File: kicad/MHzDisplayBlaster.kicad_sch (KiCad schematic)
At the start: 6 parts, among them J1 Conn_02x15 DigitRHS, J2 Conn_02x15 DigitLHS, J3 Conn_01x03, J4 Conn_01x07, U1 DC56-11GWA

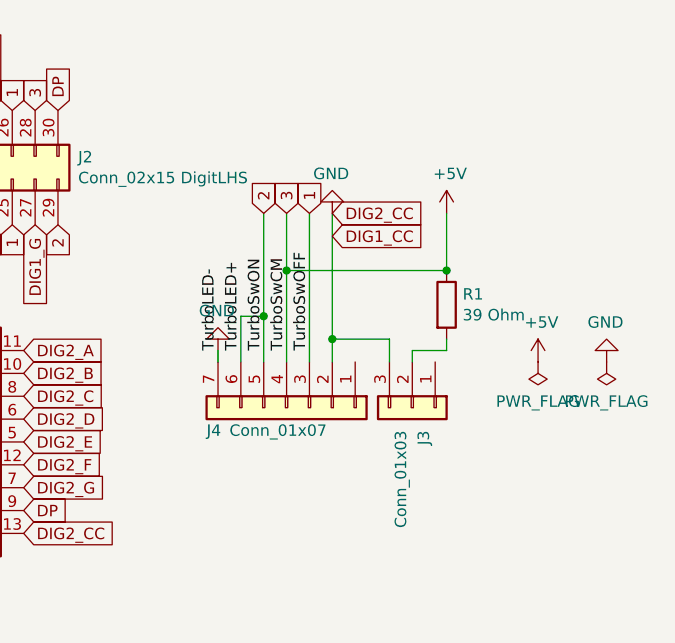
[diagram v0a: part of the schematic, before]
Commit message: Split 7-pin connector
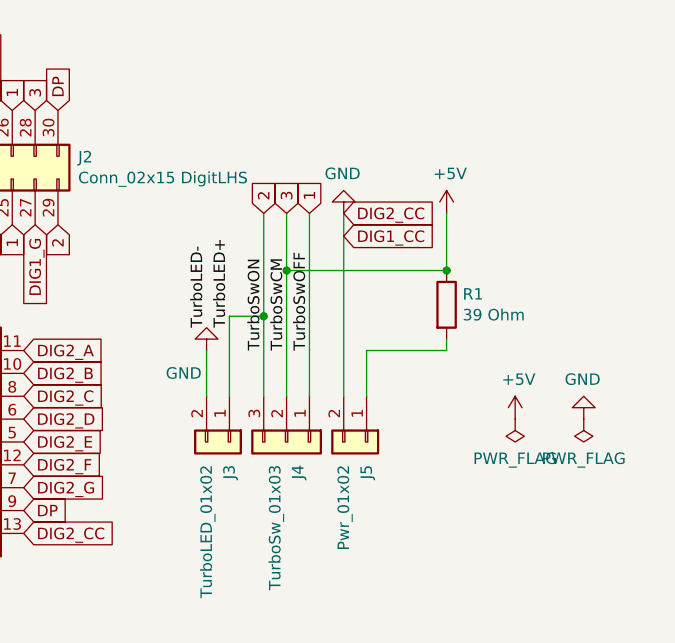
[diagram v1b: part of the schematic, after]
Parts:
- removed J4: Conn_01x07, Connector_PinHeader_2.54mm:PinHeader_1x07_P2.54mm_Vertical, symbol Connector_Generic:Conn_01x07
- added J3: TurboLED_01x02, Connector_PinHeader_2.54mm:PinHeader_1x02_P2.54mm_Vertical, symbol Connector_Generic:Conn_01x02
- added J5: Pwr_01x02, Connector_PinHeader_2.54mm:PinHeader_1x02_P2.54mm_Vertical, symbol Connector_Generic:Conn_01x02
- J4: renamed from J3; value Conn_01x03 -> TurboSw_01x03
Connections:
- net +5V: now also J4.2 (Pin_2)
- net 1: now also J4.1 (Pin_1)
- net 2: now also J4.3 (Pin_3), J3.1 (Pin_1)
- net GND: now also J3.2 (Pin_2), J5.2 (Pin_2); no longer J4.3 (Pin_3)
- net at R1.2: now also J5.1 (Pin_1); no longer J4.2 (Pin_2)
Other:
- moved on the sheet: J4

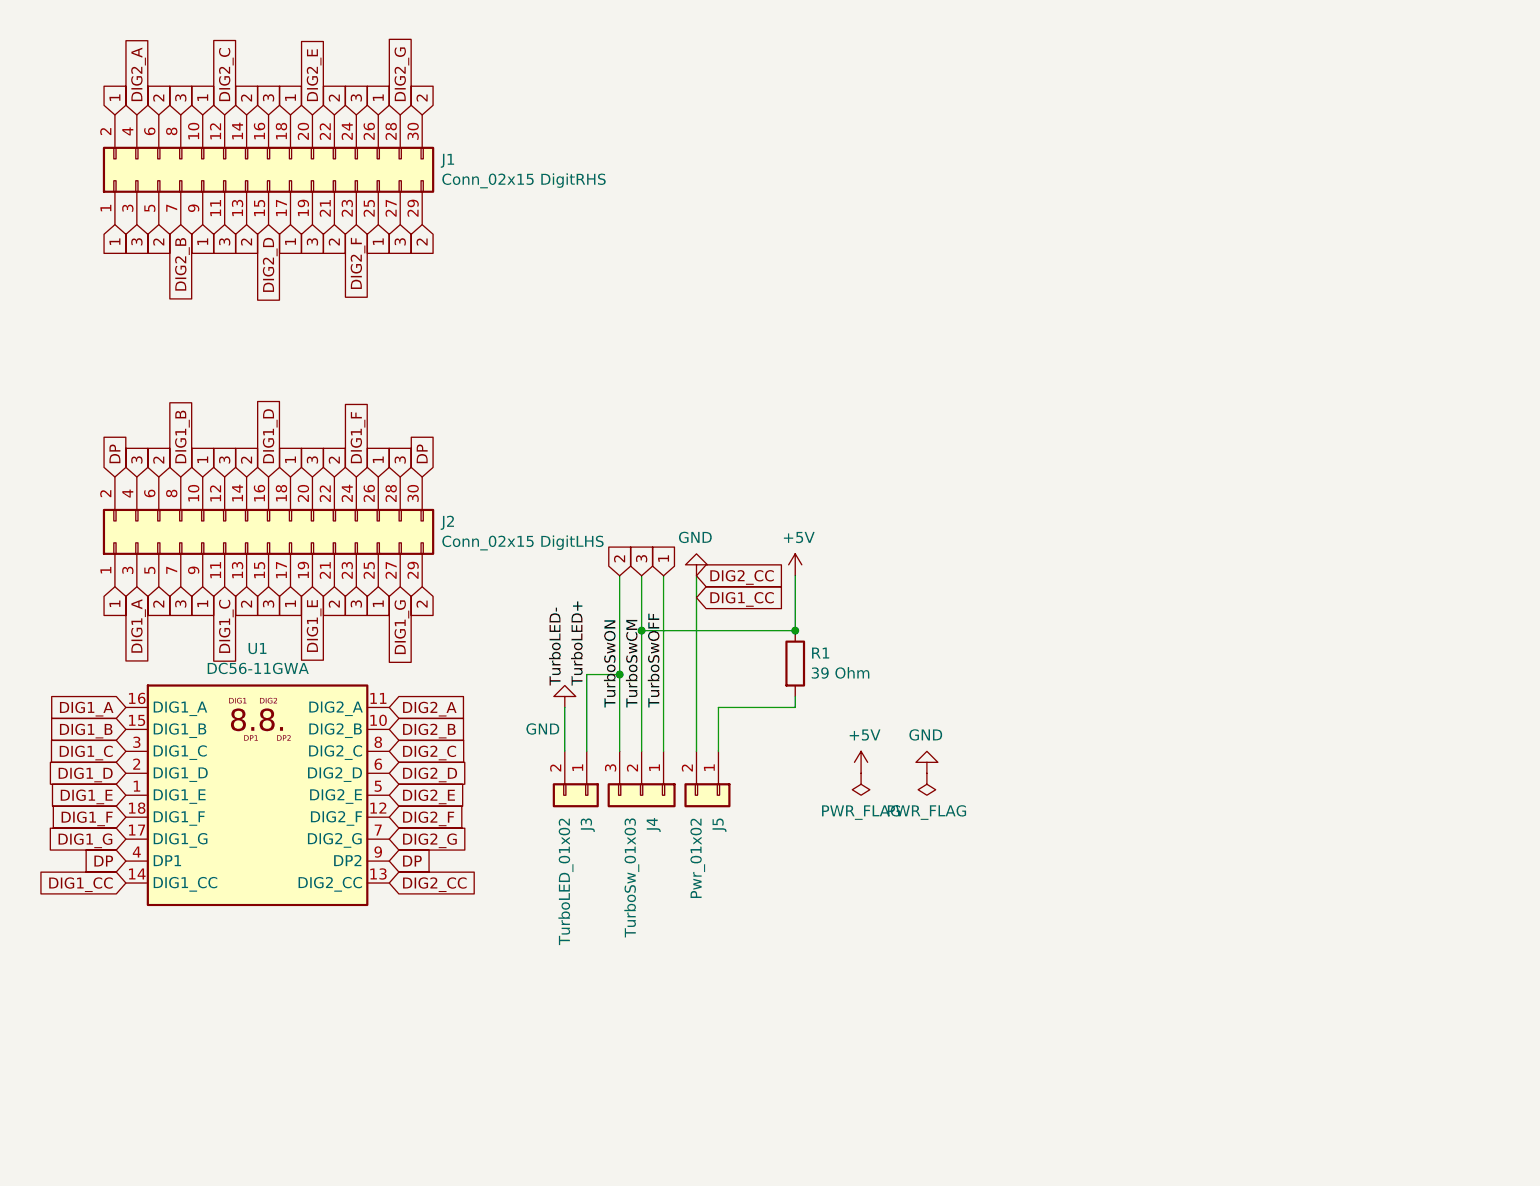
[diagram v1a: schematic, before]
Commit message: Update Schematic 74LS04
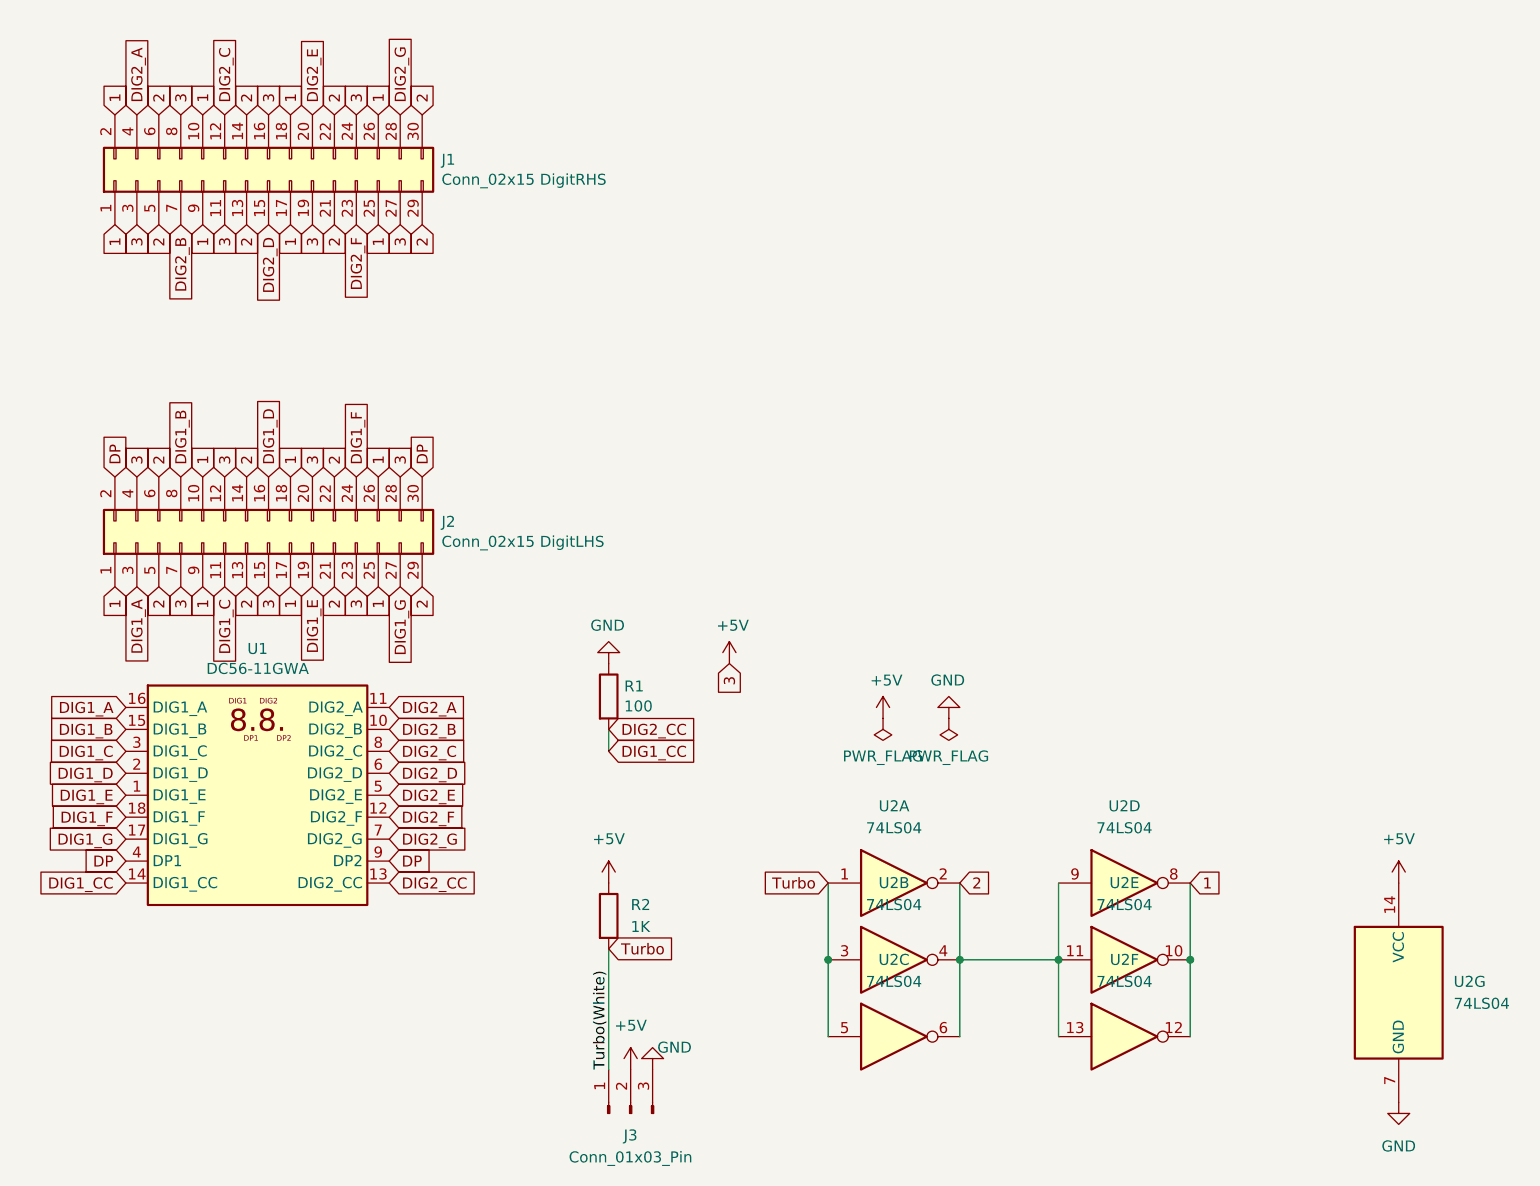
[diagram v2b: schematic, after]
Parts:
- removed J3: TurboLED_01x02, Connector_PinHeader_2.54mm:PinHeader_1x02_P2.54mm_Vertical, symbol Connector_Generic:Conn_01x02
- removed J4: TurboSw_01x03, Connector_PinHeader_2.54mm:PinHeader_1x03_P2.54mm_Vertical, symbol Connector_Generic:Conn_01x03
- removed J5: Pwr_01x02, Connector_PinHeader_2.54mm:PinHeader_1x02_P2.54mm_Vertical, symbol Connector_Generic:Conn_01x02
- added J3: Conn_01x03_Pin, Connector_PinHeader_2.54mm:PinHeader_1x03_P2.54mm_Vertical, symbol Connector:Conn_01x03_Pin
- added R2: 1K, Resistor_THT:R_Axial_DIN0207_L6.3mm_D2.5mm_P10.16mm_Horizontal, symbol Device:R
- added U2: 74LS04, Package_SO:SOIC-14_3.9x8.7mm_P1.27mm, symbol 74xx:74LS04
- R1: value 39 Ohm -> 100
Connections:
- net +5V: now also J3.2 (Pin_2), R2.1, U2.14 (VCC); no longer R1.1
- net 1: now also U2.10, U2.12, U2.8
- net 2: now also U2.11, U2.13, U2.2, U2.4, U2.6, U2.9
- net GND: now also R1.1, J3.3 (Pin_3), U2.7 (GND); no longer U1.13 (DIG2_CC), U1.14 (DIG1_CC)
- net DIG1_CC: now reaches R1.2
- net DIG1_CC: now also U1.13 (DIG2_CC), U1.14 (DIG1_CC)
- new net Turbo: J3.1 (Pin_1), R2.2, U2.1, U2.3, U2.5
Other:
- moved on the sheet: R1

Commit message: Cleanup and Routing
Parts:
- R1, R2: footprint Resistor_THT:R_Axial_DIN0207_L6.3mm_D2.5mm_P10.16mm_Horizontal -> Resistor_THT:R_Axial_DIN0204_L3.6mm_D1.6mm_P5.08mm_Horizontal
- renumbered J2 to J1, J1 to J2
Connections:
- net GND: now also J3.1 (Pin_1); no longer J3.3 (Pin_3)
- net Turbo: now also J3.3 (Pin_3); no longer J3.1 (Pin_1)
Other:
- moved on the sheet: R2
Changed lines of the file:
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@@
   (junction (at 229.87 125.73) (diameter 0) (color 0 0 0 0)
-  )
-  (wire (pts (xy 177.8 124.46) (xy 177.8 138.43))
-    (stroke (width 0) (type default))
   )
   (wire (pts (xy 203.2 125.73) (xy 203.2 134.62))
@@
     (stroke (width 0) (type default))
   )
+  (wire (pts (xy 182.88 118.11) (xy 182.88 138.43))
+    (stroke (width 0) (type default))
+  )
   (wire (pts (xy 245.11 125.73) (xy 245.11 134.62))
     (stroke (width 0) (type default))
@@
     (stroke (width 0) (type default))
   )
+  (wire (pts (xy 177.8 134.62) (xy 177.8 138.43))
+    (stroke (width 0) (type default))
+  )
   (wire (pts (xy 177.8 99.06) (xy 177.8 101.6))
     (stroke (width 0) (type default))
@@
     (stroke (width 0) (type default))
   )
-  (label "Turbo(White)" (at 177.8 138.43 90) (fields_autoplaced)
+  (label "Turbo(White)" (at 182.88 129.54 90) (fields_autoplaced)
     (effects (font (size 1.27 1.27)) (justify left bottom))
   )
@@
     )
   )
-  (global_label "Turbo" (shape input) (at 177.8 124.46 0) (fields_autoplaced)
-    (effects (font (size 1.27 1.27)) (justify left))
-    (property "Intersheetrefs" "${INTERSHEET_REFS}" (at 185.3318 124.46 0)
+  (global_label "Turbo" (shape input) (at 182.88 118.11 0) (fields_autoplaced)
+    (effects (font (size 1.27 1.27)) (justify left))
+    (property "Intersheetrefs" "${INTERSHEET_REFS}" (at 190.4118 118.11 0)
       (effects (font (size 1.27 1.27)) (justify left) hide)
     )
@@
   (symbol (lib_id "Connector_Generic:Conn_02x15_Odd_Even") (at 138.43 35.56 90) (unit 1)
     (in_bom yes) (on_board yes) (dnp no)
-    (property "Reference" "J1" (at 158.4452 33.1216 90)
+    (property "Reference" "J2" (at 158.4452 33.1216 90)
       (effects (font (size 1.27 1.27)) (justify right))
     )
@@
       (project "MHzDisplayBlaster"
         (path "/49ffe564-7955-4314-8534-74674e8c72b2"
-          (reference "J1") (unit 1)
+          (reference "J2") (unit 1)
         )
       )
@@
   (symbol (lib_id "Connector_Generic:Conn_02x15_Odd_Even") (at 138.43 77.47 90) (unit 1)
     (in_bom yes) (on_board yes) (dnp no)
-    (property "Reference" "J2" (at 158.4452 75.0316 90)
+    (property "Reference" "J1" (at 158.4452 75.0316 90)
       (effects (font (size 1.27 1.27)) (justify right))
     )
@@
       (project "MHzDisplayBlaster"
         (path "/49ffe564-7955-4314-8534-74674e8c72b2"
-          (reference "J2") (unit 1)
+          (reference "J1") (unit 1)
         )
       )
@@
       (effects (font (size 1.27 1.27)) (justify left))
     )
-    (property "Footprint" "Resistor_THT:R_Axial_DIN0207_L6.3mm_D2.5mm_P10.16mm_Horizontal" (at 176.022 95.25 90)
+    (property "Footprint" "Resistor_THT:R_Axial_DIN0204_L3.6mm_D1.6mm_P5.08mm_Horizontal" (at 176.022 95.25 90)
       (effects (font (size 1.27 1.27)) hide)
     )
@@
     )
   )
-  (symbol (lib_id "Device:R") (at 177.8 120.65 0) (unit 1)
+  (symbol (lib_id "Device:R") (at 182.88 114.3 0) (unit 1)
     (in_bom yes) (on_board yes) (dnp no) (fields_autoplaced)
-    (property "Reference" "R2" (at 180.34 119.38 0)
+    (property "Reference" "R2" (at 185.42 113.03 0)
       (effects (font (size 1.27 1.27)) (justify left))
     )
-    (property "Value" "1K" (at 180.34 121.92 0)
+    (property "Value" "1K" (at 185.42 115.57 0)
       (effects (font (size 1.27 1.27)) (justify left))
     )
-    (property "Footprint" "Resistor_THT:R_Axial_DIN0207_L6.3mm_D2.5mm_P10.16mm_Horizontal" (at 176.022 120.65 90)
-      (effects (font (size 1.27 1.27)) hide)
-    )
-    (property "Datasheet" "~" (at 177.8 120.65 0)
+    (property "Footprint" "Resistor_THT:R_Axial_DIN0204_L3.6mm_D1.6mm_P5.08mm_Horizontal" (at 181.102 114.3 90)
+      (effects (font (size 1.27 1.27)) hide)
+    )
+    (property "Datasheet" "~" (at 182.88 114.3 0)
       (effects (font (size 1.27 1.27)) hide)
     )
@@
     )
   )
-  (symbol (lib_id "power:GND") (at 182.88 138.43 180) (unit 1)
+  (symbol (lib_id "power:GND") (at 177.8 134.62 180) (unit 1)
     (in_bom yes) (on_board yes) (dnp no)
-    (property "Reference" "#PWR07" (at 182.88 132.08 0)
-      (effects (font (size 1.27 1.27)) hide)
-    )
-    (property "Value" "GND" (at 185.42 135.89 0)
-      (effects (font (size 1.27 1.27)))
-    )
-    (property "Footprint" "" (at 182.88 138.43 0)
-      (effects (font (size 1.27 1.27)) hide)
-    )
-    (property "Datasheet" "" (at 182.88 138.43 0)
+    (property "Reference" "#PWR07" (at 177.8 128.27 0)
+      (effects (font (size 1.27 1.27)) hide)
+    )
+    (property "Value" "GND" (at 180.34 132.08 0)
+      (effects (font (size 1.27 1.27)) (justify left top))
+    )
+    (property "Footprint" "" (at 177.8 134.62 0)
+      (effects (font (size 1.27 1.27)) hide)
+    )
+    (property "Datasheet" "" (at 177.8 134.62 0)
       (effects (font (size 1.27 1.27)) hide)
     )
@@
     )
   )
-  (symbol (lib_id "power:+5V") (at 177.8 116.84 0) (unit 1)
+  (symbol (lib_id "power:+5V") (at 182.88 110.49 0) (unit 1)
     (in_bom yes) (on_board yes) (dnp no)
-    (property "Reference" "#PWR05" (at 177.8 120.65 0)
-      (effects (font (size 1.27 1.27)) hide)
-    )
-    (property "Value" "+5V" (at 177.8 111.76 0)
-      (effects (font (size 1.27 1.27)))
-    )
-    (property "Footprint" "" (at 177.8 116.84 0)
-      (effects (font (size 1.27 1.27)) hide)
-    )
-    (property "Datasheet" "" (at 177.8 116.84 0)
-      (effects (font (size 1.27 1.27)) hide)
-    )
+    (property "Reference" "#PWR05" (at 182.88 114.3 0)
+      (effects (font (size 1.27 1.27)) hide)
+    )
+    (property "Value" "+5V" (at 182.88 105.41 0)
+      (effects (font (size 1.27 1.27)))
+    )
+    (property "Footprint" "" (at 182.88 110.49 0)
+      (effects (font (size 1.27 1.27)) hide)
+    )
+    (property "Datasheet" "" (at 182.88 110.49 0)
+      (effects (font (size 1.27 1.27)) hide)
+    )

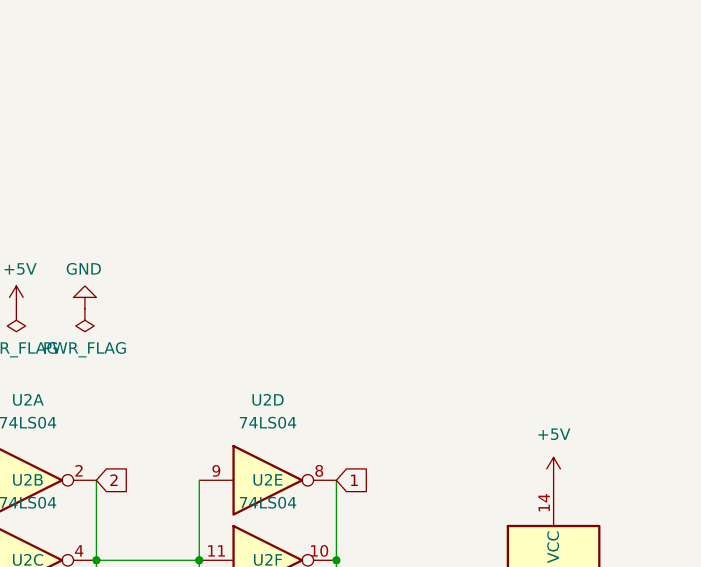
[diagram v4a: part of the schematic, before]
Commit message: Add Turbo LED Header
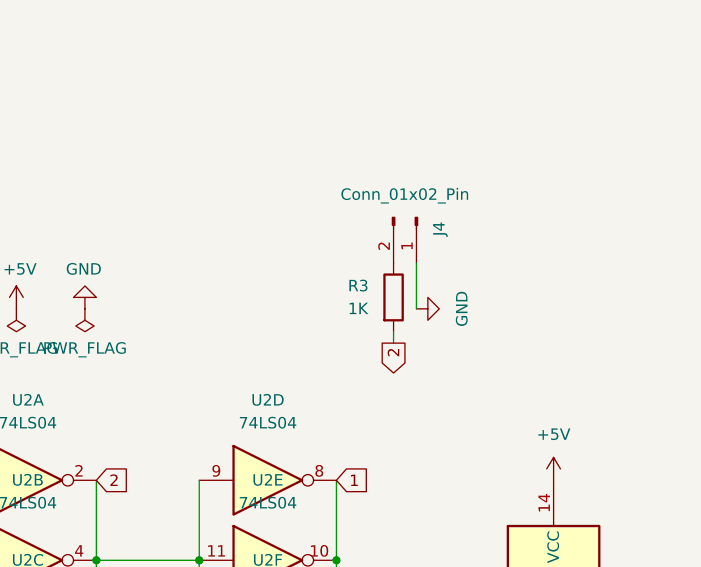
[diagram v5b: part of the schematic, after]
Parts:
- added J4: Conn_01x02_Pin, Connector_PinHeader_2.54mm:PinHeader_1x02_P2.54mm_Vertical, symbol Connector:Conn_01x02_Pin
- added R3: 1K, Resistor_THT:R_Axial_DIN0204_L3.6mm_D1.6mm_P5.08mm_Horizontal, symbol Device:R
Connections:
- net 2: now also R3.2
- net GND: now also J4.1 (Pin_1)
- new net: J4.2 (Pin_2), R3.1
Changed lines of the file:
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@@
+    (stroke (width 0) (type default))
+  )
+  (wire (pts (xy 251.46 101.6) (xy 251.46 100.33))
     (stroke (width 0) (type default))
   )
@@
     (stroke (width 0) (type default))
   )
+  (wire (pts (xy 254 92.71) (xy 254 97.79))
+    (stroke (width 0) (type default))
+  )
   (wire (pts (xy 177.8 99.06) (xy 177.8 101.6))
     (stroke (width 0) (type default))
@@
     (effects (font (size 1.27 1.27)) (justify right))
     (property "Intersheetrefs" "${INTERSHEET_REFS}" (at 121.92 104.14 0)
+      (effects (font (size 1.27 1.27)) hide)
+    )
+  )
+  (global_label "2" (shape output) (at 251.46 101.6 270)
+    (effects (font (size 1.27 1.27)) (justify right))
+    (property "Intersheetrefs" "${INTERSHEET_REFS}" (at 251.46 101.6 0)
       (effects (font (size 1.27 1.27)) hide)
     )
@@
     )
   )
+  (symbol (lib_id "Connector:Conn_01x02_Pin") (at 254 87.63 270) (unit 1)
+    (in_bom yes) (on_board yes) (dnp no)
+    (property "Reference" "J4" (at 256.54 88.9 0)
+      (effects (font (size 1.27 1.27)))
+    )
+    (property "Value" "Conn_01x02_Pin" (at 252.73 85.09 90)
+      (effects (font (size 1.27 1.27)))
+    )
+    (property "Footprint" "Connector_PinHeader_2.54mm:PinHeader_1x02_P2.54mm_Vertical" (at 254 87.63 0)
+      (effects (font (size 1.27 1.27)) hide)
+    )
+    (property "Datasheet" "~" (at 254 87.63 0)
+      (effects (font (size 1.27 1.27)) hide)
+    )
+    (pin "1")
+    (pin "2")
+    (instances
+      (project "MHzDisplayBlaster"
+        (path "/49ffe564-7955-4314-8534-74674e8c72b2"
+          (reference "J4") (unit 1)
+        )
+      )
+    )
+  )
+  (symbol (lib_id "power:GND") (at 254 97.79 90) (unit 1)
+    (in_bom yes) (on_board yes) (dnp no) (fields_autoplaced)
+    (property "Reference" "#PWR08" (at 260.35 97.79 0)
+      (effects (font (size 1.27 1.27)) hide)
+    )
+    (property "Value" "GND" (at 259.08 97.79 0)
+      (effects (font (size 1.27 1.27)))
+    )
+    (property "Footprint" "" (at 254 97.79 0)
+      (effects (font (size 1.27 1.27)) hide)
+    )
+    (property "Datasheet" "" (at 254 97.79 0)
+      (effects (font (size 1.27 1.27)) hide)
+    )
+    (pin "1")
+    (instances
+      (project "MHzDisplayBlaster"
+        (path "/49ffe564-7955-4314-8534-74674e8c72b2"
+          (reference "#PWR08") (unit 1)
+        )
+      )
+    )
+  )
   (symbol (lib_id "Connector:Conn_01x03_Pin") (at 180.34 143.51 90) (unit 1)
     (in_bom yes) (on_board yes) (dnp no) (fields_autoplaced)
@@
         )
       )
+    )
+  )
+  (symbol (lib_id "Device:R") (at 251.46 96.52 0) (unit 1)
+    (in_bom yes) (on_board yes) (dnp no)
+    (property "Reference" "R3" (at 246.38 95.25 0)
+      (effects (font (size 1.27 1.27)) (justify left))
+    )
+    (property "Value" "1K" (at 246.38 97.79 0)
+      (effects (font (size 1.27 1.27)) (justify left))
+    )
+    (property "Footprint" "Resistor_THT:R_Axial_DIN0204_L3.6mm_D1.6mm_P5.08mm_Horizontal" (at 249.682 96.52 90)
+      (effects (font (size 1.27 1.27)) hide)
+    )
+    (property "Datasheet" "~" (at 251.46 96.52 0)
+      (effects (font (size 1.27 1.27)) hide)
+    )
+    (pin "1")
+    (pin "2")
+    (instances
+      (project "MHzDisplayBlaster"
+        (path "/49ffe564-7955-4314-8534-74674e8c72b2"
+          (reference "R3") (unit 1)
+        )
+      )
